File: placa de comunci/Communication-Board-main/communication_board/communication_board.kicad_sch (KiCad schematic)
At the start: 58 parts, among them J1 USB_IN, J10 B4B-XH-A, J11 B4B-XH-A, J12 XT60-M, J13 B4B-XH-A, J14 B4B-XH-A, J15 B4B-XH-A, J16 B4B-XH-A, J17 B4B-XH-A, J2 IMU, J3 MINI_FUSE, J4 Motors, J5 XT60-M, J6 XT60-M, J7 B4B-XH-A, J8 B4B-XH-A, J9 B4B-XH-A, SW1 SW_DPST_x2, U1 FE1.1s, U2 FT232RL, U3 FT232RL, U4 MAX485E, Y1 Crystal

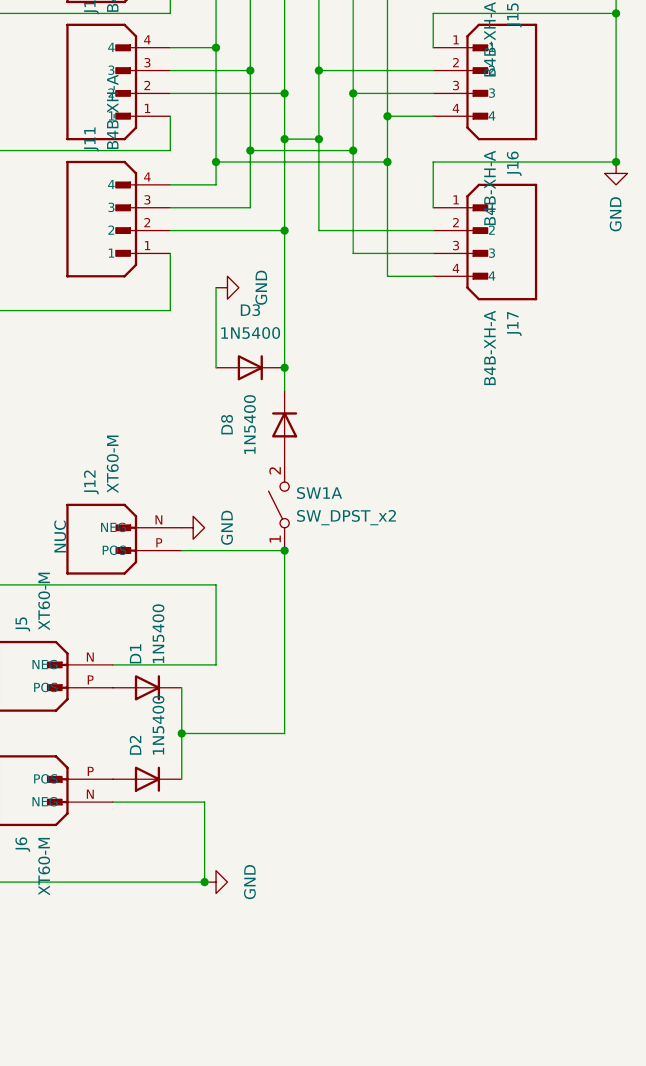
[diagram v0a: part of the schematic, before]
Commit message: imu nova (MPU6050)
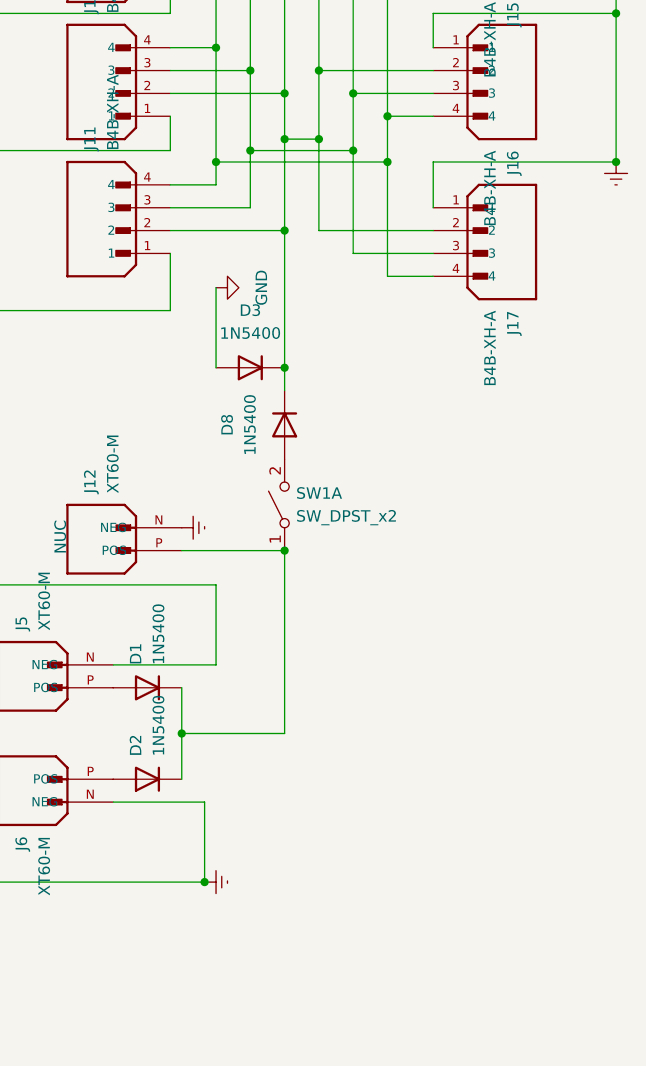
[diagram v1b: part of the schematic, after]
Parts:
- SW1: footprint Button_Switch_THT:SW_DIP_SPSTx01_Slide_9.78x4.72mm_W7.62mm_P2.54mm -> Connector_Pin:Pin_D1.1mm_L10.2mm_W3.5mm_Flat
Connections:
- net GND: no longer J10.1, J11.1, J12.N (NEG), J13.1, J14.1, J15.1, J16.1, J17.1, J5.N (NEG), J6.N (NEG), J7.1, J8.1, J9.1
- net GNDREF: now also J10.1, J11.1, J12.N (NEG), J13.1, J14.1, J15.1, J16.1, J17.1, J5.N (NEG), J6.N (NEG), J7.1, J8.1, J9.1
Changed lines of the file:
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@@
 	)
 	(junction
+		(at 275.59 83.82)
+		(diameter 0)
+		(color 0 0 0 0)
+	)
+	(junction
 		(at 275.59 33.02)
 		(diameter 0)
@@
 	)
 	(junction
+		(at 229.87 163.83)
+		(diameter 0)
+		(color 0 0 0 0)
+	)
+	(junction
 		(at 162.56 55.245)
 		(diameter 0)
@@
 	)
 	(junction
-		(at 229.87 163.83)
-		(diameter 0)
-		(color 0 0 0 0)
-	)
-	(junction
 		(at 231.14 40.64)
 		(diameter 0)
@@
 	)
 	(junction
-		(at 275.59 83.82)
-		(diameter 0)
-		(color 0 0 0 0)
-	)
-	(junction
 		(at 67.31 29.21)
 		(diameter 0)
@@
 	)
 	(symbol
-		(lib_id "power:GND")
-		(at 227.33 124.46 90)
-		(unit 1)
-		(exclude_from_sim no)
-		(in_bom yes)
-		(on_board yes)
-		(dnp no)
-		(fields_autoplaced yes)
-		(property "Reference" "#PWR018"
-			(at 233.68 124.46 0)
-			(effects
-				(font
-					(size 1.27 1.27)
-				)
-				(hide yes)
-			)
-		)
-		(property "Value" "GND"
-			(at 232.41 124.46 0)
-			(effects
-				(font
-					(size 1.27 1.27)
-				)
-			)
-		)
-		(property "Footprint" ""
-			(at 227.33 124.46 0)
-			(effects
-				(font
-					(size 1.27 1.27)
-				)
-				(hide yes)
-			)
-		)
-		(property "Datasheet" ""
-			(at 227.33 124.46 0)
-			(effects
-				(font
-					(size 1.27 1.27)
-				)
-				(hide yes)
-			)
-		)
-		(property "Description" "Power symbol creates a global label with name \"GND\" , ground"
-			(at 227.33 124.46 0)
-			(effects
-				(font
-					(size 1.27 1.27)
-				)
-				(hide yes)
-			)
-		)
-		(pin "1"
-		)
-		(instances
-			(project "communication_board"
-				(path "/541a1e5d-fb77-41a5-941f-f895851ed477"
-					(reference "#PWR018")
-					(unit 1)
-				)
-			)
-		)
-	)
-	(symbol
 		(lib_id "Device:R")
 		(at 117.475 60.325 90)
@@
 			)
 		)
-		(property "Footprint" "Button_Switch_THT:SW_DIP_SPSTx01_Slide_9.78x4.72mm_W7.62mm_P2.54mm"
+		(property "Footprint" "Connector_Pin:Pin_D1.1mm_L10.2mm_W3.5mm_Flat"
 			(at 238.76 121.92 0)
 			(effects
@@
 	)
 	(symbol
-		(lib_id "power:GND")
-		(at 229.87 163.83 90)
-		(unit 1)
-		(exclude_from_sim no)
-		(in_bom yes)
-		(on_board yes)
-		(dnp no)
-		(fields_autoplaced yes)
-		(property "Reference" "#PWR019"
-			(at 236.22 163.83 0)
-			(effects
-				(font
-					(size 1.27 1.27)
-				)
-				(hide yes)
-			)
-		)
-		(property "Value" "GND"
-			(at 234.95 163.83 0)
-			(effects
-				(font
-					(size 1.27 1.27)
-				)
-			)
-		)
-		(property "Footprint" ""
-			(at 229.87 163.83 0)
-			(effects
-				(font
-					(size 1.27 1.27)
-				)
-				(hide yes)
-			)
-		)
-		(property "Datasheet" ""
-			(at 229.87 163.83 0)
-			(effects
-				(font
-					(size 1.27 1.27)
-				)
-				(hide yes)
-			)
-		)
-		(property "Description" "Power symbol creates a global label with name \"GND\" , ground"
-			(at 229.87 163.83 0)
-			(effects
-				(font
-					(size 1.27 1.27)
-				)
-				(hide yes)
-			)
-		)
-		(pin "1"
-		)
-		(instances
-			(project "communication_board"
-				(path "/541a1e5d-fb77-41a5-941f-f895851ed477"
-					(reference "#PWR019")
-					(unit 1)
-				)
-			)
-		)
-	)
-	(symbol
 		(lib_id "Device:C")
 		(at 27.94 68.58 90)
@@
 	(symbol
 		(lib_id "power:GNDREF")
+		(at 229.87 163.83 90)
+		(unit 1)
+		(exclude_from_sim no)
+		(in_bom yes)
+		(on_board yes)
+		(dnp no)
+		(fields_autoplaced yes)
+		(property "Reference" "#PWR019"
+			(at 236.22 163.83 0)
+			(effects
+				(font
+					(size 1.27 1.27)
+				)
+				(hide yes)
+			)
+		)
+		(property "Value" "GNDREF"
+			(at 234.315 163.83 0)
+			(effects
+				(font
+					(size 1.27 1.27)
+				)
+				(hide yes)
+			)
+		)
+		(property "Footprint" ""
+			(at 229.87 163.83 0)
+			(effects
+				(font
+					(size 1.27 1.27)
+				)
+				(hide yes)
+			)
+		)
+		(property "Datasheet" ""
+			(at 229.87 163.83 0)
+			(effects
+				(font
+					(size 1.27 1.27)
+				)
+				(hide yes)
+			)
+		)
+		(property "Description" ""
+			(at 229.87 163.83 0)
+			(effects
+				(font
+					(size 1.27 1.27)
+				)
+				(hide yes)
+			)
+		)
+		(pin "1"
+		)
+		(instances
+			(project "communication_board"
+				(path "/541a1e5d-fb77-41a5-941f-f895851ed477"
+					(reference "#PWR019")
+					(unit 1)
+				)
+			)
+		)
+	)
+	(symbol
+		(lib_id "power:GNDREF")
 		(at 123.19 120.015 0)
 		(unit 1)
@@
 	)
 	(symbol
+		(lib_id "power:GNDREF")
+		(at 275.59 83.82 0)
+		(unit 1)
+		(exclude_from_sim no)
+		(in_bom yes)
+		(on_board yes)
+		(dnp no)
+		(fields_autoplaced yes)
+		(property "Reference" "#PWR022"
+			(at 275.59 90.17 0)
+			(effects
+				(font
+					(size 1.27 1.27)
+				)
+				(hide yes)
+			)
+		)
+		(property "Value" "GNDREF"
+			(at 275.59 88.265 0)
+			(effects
+				(font
+					(size 1.27 1.27)
+				)
+				(hide yes)
+			)
+		)
+		(property "Footprint" ""
+			(at 275.59 83.82 0)
+			(effects
+				(font
+					(size 1.27 1.27)
+				)
+				(hide yes)
+			)
+		)
+		(property "Datasheet" ""
+			(at 275.59 83.82 0)
+			(effects
+				(font
+					(size 1.27 1.27)
+				)
+				(hide yes)
+			)
+		)
+		(property "Description" ""
+			(at 275.59 83.82 0)
+			(effects
+				(font
+					(size 1.27 1.27)
+				)
+				(hide yes)
+			)
+		)
+		(pin "1"
+		)
+		(instances
+			(project "communication_board"
+				(path "/541a1e5d-fb77-41a5-941f-f895851ed477"
+					(reference "#PWR022")
+					(unit 1)
+				)
+			)
+		)
+	)
+	(symbol
 		(lib_id "Diode:1N5400")
 		(at 223.52 142.24 180)
@@
 	)
 	(symbol
-		(lib_id "power:GND")
-		(at 275.59 83.82 0)
-		(unit 1)
-		(exclude_from_sim no)
-		(in_bom yes)
-		(on_board yes)
-		(dnp no)
-		(fields_autoplaced yes)
-		(property "Reference" "#PWR021"
-			(at 275.59 90.17 0)
-			(effects
-				(font
-					(size 1.27 1.27)
-				)
-				(hide yes)
-			)
-		)
-		(property "Value" "GND"
-			(at 275.5901 87.63 90)
-			(effects
-				(font
-					(size 1.27 1.27)
-				)
-				(justify right)
-			)
-		)
-		(property "Footprint" ""
-			(at 275.59 83.82 0)
-			(effects
-				(font
-					(size 1.27 1.27)
-				)
-				(hide yes)
-			)
-		)
-		(property "Datasheet" ""
-			(at 275.59 83.82 0)
-			(effects
-				(font
-					(size 1.27 1.27)
-				)
-				(hide yes)
-			)
-		)
-		(property "Description" "Power symbol creates a global label with name \"GND\" , ground"
-			(at 275.59 83.82 0)
-			(effects
-				(font
-					(size 1.27 1.27)
-				)
-				(hide yes)
-			)
-		)
-		(pin "1"
-		)
-		(instances
-			(project "communication_board"
-				(path "/541a1e5d-fb77-41a5-941f-f895851ed477"
-					(reference "#PWR021")
-					(unit 1)
-				)
-			)
-		)
-	)
-	(symbol
 		(lib_id "Interface_USB:FT232RL")
 		(at 55.88 86.36 0)
@@
 					(unit 1)
 				)
+			)
+		)
+	)
+	(symbol
+		(lib_id "power:GNDREF")
+		(at 227.33 124.46 90)
+		(unit 1)
+		(exclude_from_sim no)
+		(in_bom yes)
+		(on_board yes)
+		(dnp no)
+		(fields_autoplaced yes)
+		(property "Reference" "#PWR018"
+			(at 233.68 124.46 0)
+			(effects
+				(font
+					(size 1.27 1.27)
+				)
+				(hide yes)
+			)
+		)
+		(property "Value" "GNDREF"
+			(at 231.775 124.46 0)
+			(effects
+				(font
+					(size 1.27 1.27)
+				)
+				(hide yes)
+			)
+		)
+		(property "Footprint" ""
+			(at 227.33 124.46 0)
+			(effects
+				(font
+					(size 1.27 1.27)
+				)
+				(hide yes)
+			)
+		)
+		(property "Datasheet" ""
+			(at 227.33 124.46 0)
+			(effects
+				(font
+					(size 1.27 1.27)
+				)
+				(hide yes)
+			)
+		)
+		(property "Description" ""
+			(at 227.33 124.46 0)
+			(effects
+				(font
+					(size 1.27 1.27)
+				)
+				(hide yes)
+			)
+		)
+		(pin "1"
+		)
+		(instances
+			(project "communication_board"
+				(path "/541a1e5d-fb77-41a5-941f-f895851ed477"
+					(reference "#PWR018")
+					(unit 1)
+				)
